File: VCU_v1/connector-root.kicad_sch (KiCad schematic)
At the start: 4 parts, among them J1 Micro_SD_Card, U4 MX150 20-pin, U5 MX150 20-pin, U6 MX150 20-pin

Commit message: p dih r
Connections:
- net SPEAKER+: now reaches U5.1
- net BMS-FAULT: now reaches U5.10
- net SPEAKER-: now reaches U5.11
- net BSPD-FAULT: now reaches U5.8
- net IMD-FAULT: now reaches U5.9
- net APPS1-SIG: now reaches U4.1
- net APPS1-4.8V: now reaches U4.10
- net BSE-GND: now reaches U4.18
- net APPS2-GND: now reaches U4.19
- net APPS1-GND: now reaches U4.20
- net APPS2-SIG: now reaches U4.3
- net BSE-SIG: now reaches U4.5
- net BSE-4.8V: now reaches U4.8
- net APPS2-4.8V: now reaches U4.9
- net GEN_DB1+ renamed BRAKE_LIGHT
- net GEN_DB1-: no longer names the net of U6.17
- no-connect marks 0 -> 5
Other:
- moved on the sheet: U4, U5

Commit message: v1 schematic (actually) complete, let the layout commence
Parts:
- added TP42, TP43, TP44, TP45, TP46, TP47: RH-5015, TestPoint:TestPoint_Keystone_5015_Micro_Mini, symbol .Test-Point:RH-5015
- J4: renamed from J1; footprint (none) -> Connector_Card:microSD_HC_Wuerth_693072010801; Mouser P/N (none) -> 710-693072010801
- U6: renamed from U4; footprint (none) -> 20pinMX150Header:CONN_SD-34829-001_20_ST_MOL
- U7: renamed from U5; footprint (none) -> 20pinMX150Header:CONN_SD-34829-001_20_ST_MOL
- U8: renamed from U6; footprint (none) -> 20pinMX150Header:CONN_SD-34829-001_20_ST_MOL
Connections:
- net uSD_CLK: now also TP45.1
- net uSD_CMD: now also TP44.1
- net uSD_D0: now also TP46.1
- net uSD_D1: now also TP47.1
- net uSD_D2: now also TP42.1
- net uSD_D3: now also TP43.1
- net GPIO_12: now reaches U7.12
- net GPIO_13: now reaches U7.13
- net GPIO_14: now reaches U7.14
- net GPIO_15: now reaches U7.15
- net GPIO_16: now reaches U7.16
- net GPIO_17: now reaches U7.17
- net GPIO_18: now reaches U7.18
- net GPIO_19: now reaches U7.19
- net GPIO_PWM_4: now reaches U7.2
- net GPIO_20: now reaches U7.20
- net GPIO_7: now reaches U7.3
- net GPIO_8: now reaches U7.4
- net GPIO_9: now reaches U7.5
- net GPIO_10: now reaches U7.6
- net GPIO_11: now reaches U7.7
- net GPIO_PWM_3: now reaches U8.17
- net GEN_DB2+ renamed GPIO_6
- net GEN_DB2- renamed GPIO_PWM_2
- net GEN_DB3+ renamed GPIO_5
- net GEN_DB3- renamed GPIO_PWM_1
- no-connect marks 5 -> 11
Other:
- note added: "Dash I/Os"
- note removed: "Dash GPIOs"

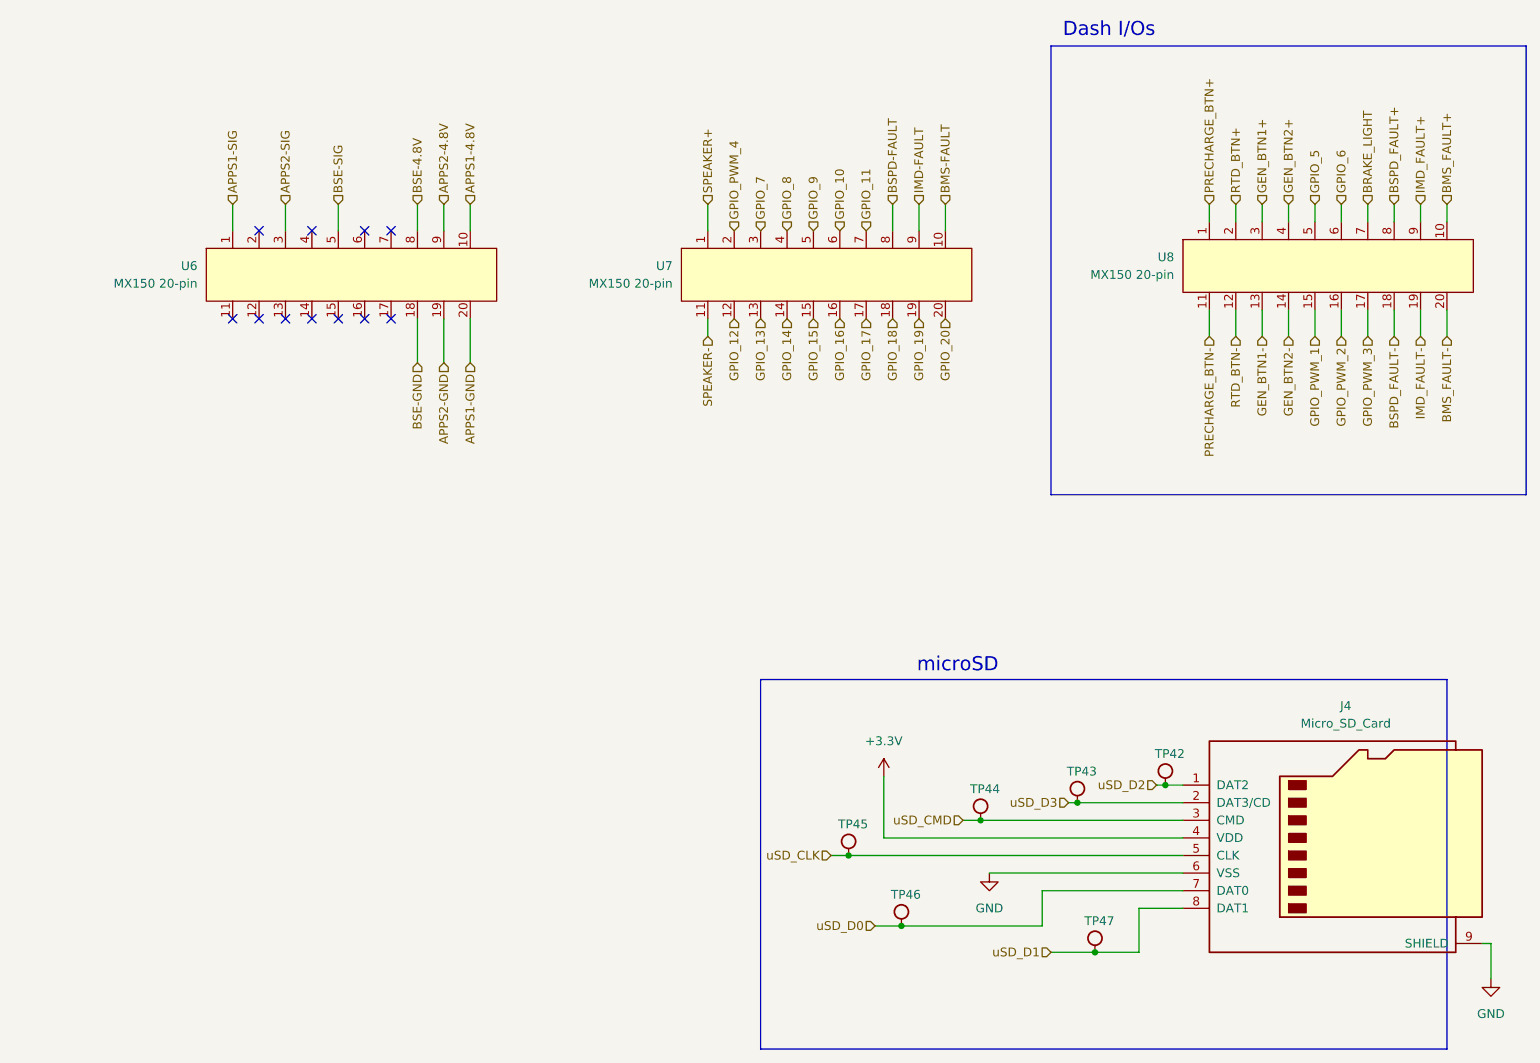
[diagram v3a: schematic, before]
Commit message: vcu placements complete
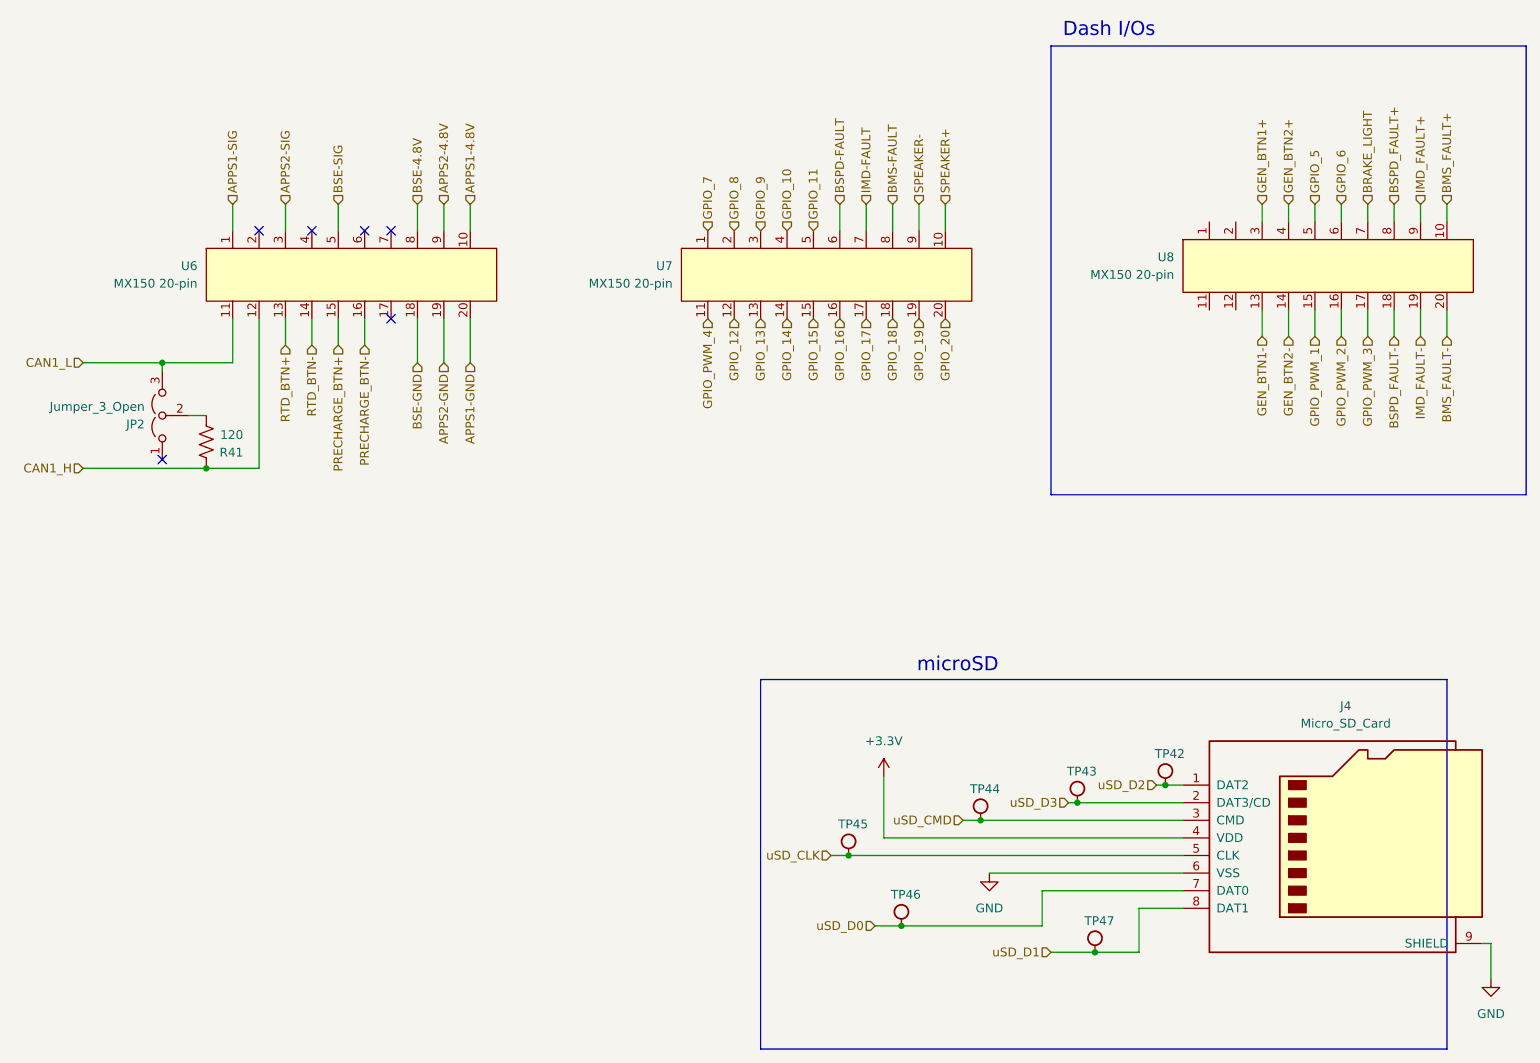
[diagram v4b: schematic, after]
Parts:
- added JP2: Jumper_3_Open, Connector_PinHeader_2.54mm:PinHeader_1x03_P2.54mm_Vertical, symbol Jumper:Jumper_3_Open
- added R41: 120, Resistor_SMD:R_0603_1608Metric_Pad0.98x0.95mm_HandSolder, symbol BFR Resistors:RMCF0603FT120R
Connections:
- net BMS-FAULT: now also U7.8; no longer U7.10
- net BSPD-FAULT: now also U7.6; no longer U7.8
- net GPIO_10: now also U7.4; no longer U7.6
- net GPIO_11: now also U7.5; no longer U7.7
- net GPIO_7: now also U7.1; no longer U7.3
- net GPIO_8: now also U7.2; no longer U7.4
- net GPIO_9: now also U7.3; no longer U7.5
- net GPIO_PWM_4: now also U7.11; no longer U7.2
- net IMD-FAULT: now also U7.7; no longer U7.9
- net PRECHARGE_BTN+: now also U6.15; no longer U8.1
- net PRECHARGE_BTN-: now also U6.16; no longer U8.11
- net RTD_BTN+: now also U6.13; no longer U8.2
- net RTD_BTN-: now also U6.14; no longer U8.12
- net SPEAKER+: now also U7.10; no longer U7.1
- net SPEAKER-: now also U7.9; no longer U7.11
- net CAN1_L: now reaches U6.11
- net CAN1_L: now also JP2.3 (B)
- net CAN1_H: now reaches U6.12
- net CAN1_H: now also R41.1
- new net: JP2.2 (C), R41.2
- no-connect marks 11 -> 6

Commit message: aughhhh
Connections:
- no-connect marks 6 -> 10
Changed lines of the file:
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@@
+	)
+	(no_connect
+		(at 240.03 44.45)
 	)
 	(no_connect
 		(at 99.06 45.72)
+	)
+	(no_connect
+		(at 236.22 44.45)
+	)
+	(no_connect
+		(at 240.03 57.15)
 	)
 	(no_connect
@@
 	)
 	(no_connect
+		(at 236.22 57.15)
+	)
+	(no_connect

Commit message: almost done i promise
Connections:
- net GPIO_10: now also U7.17; no longer U7.4
- net GPIO_11: now also U7.16; no longer U7.5
- net GPIO_12: now also U7.15; no longer U7.12
- net GPIO_13: now also U7.4; no longer U7.13
- net GPIO_15: now also U7.2; no longer U7.15
- net GPIO_16: now also U7.13; no longer U7.16
- net GPIO_17: now also U7.3; no longer U7.17
- net GPIO_18: now also U7.12; no longer U7.18
- net GPIO_7: now also U6.7; no longer U7.1
- net GPIO_8: now also U7.5; no longer U7.2
- net GPIO_9: now also U7.18; no longer U7.3
- net GPIO_PWM_1: now also U8.17; no longer U8.15
- net GPIO_PWM_3: now also U8.15; no longer U8.17
- net GPIO_PWM_4: now also U6.17; no longer U7.11
- new net Vin+: U7.1
- new net Vin-: U7.11
- no-connect marks 10 -> 8

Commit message: fixing drc errors, done besides that
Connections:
- net GPIO_12: now also U7.4; no longer U7.15
- net GPIO_13: now also U7.15; no longer U7.4
- net GPIO_15: now also U7.3; no longer U7.2
- net GPIO_17: now also U7.2; no longer U7.3
